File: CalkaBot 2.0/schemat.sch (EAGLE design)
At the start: 57 parts, among them IC1 TB6612FNG, IC2 LM339D, IC3 7806DT, Q1 16MHz, X1 MINI-USB_4P-85-32004-40X

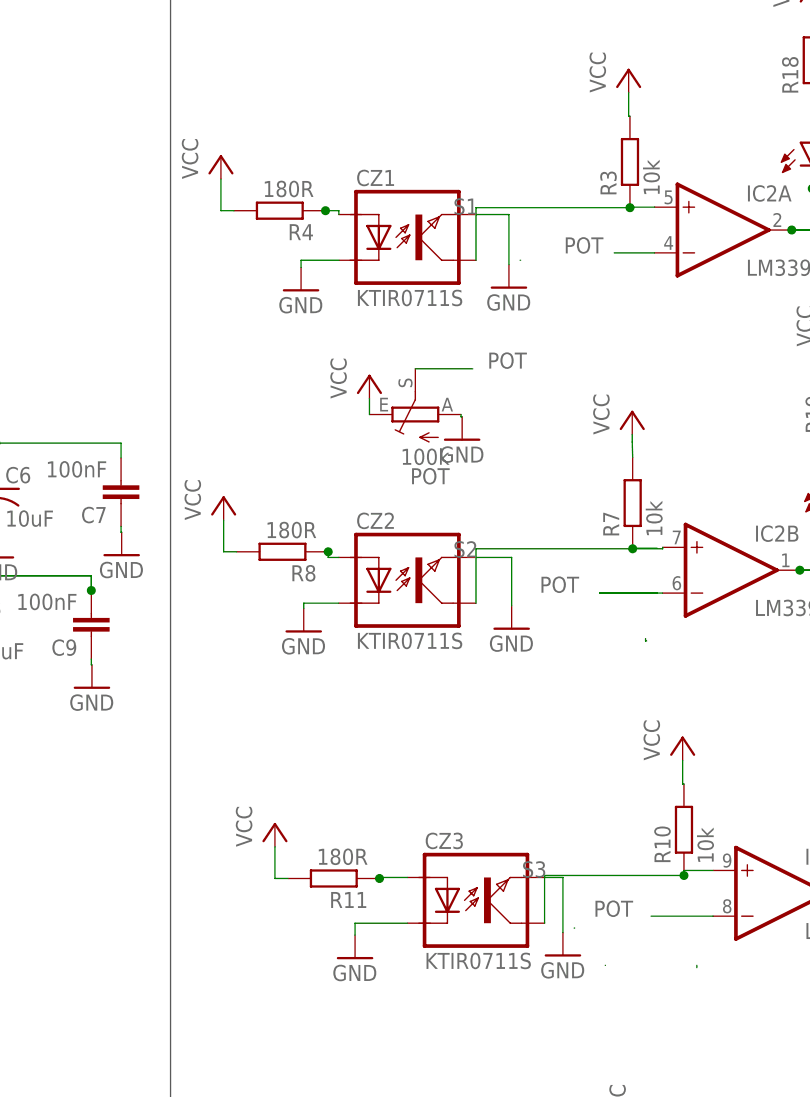
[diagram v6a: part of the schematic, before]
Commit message: Podłączone transoptory, trzeba rozkminić jak podłączyć gniazda
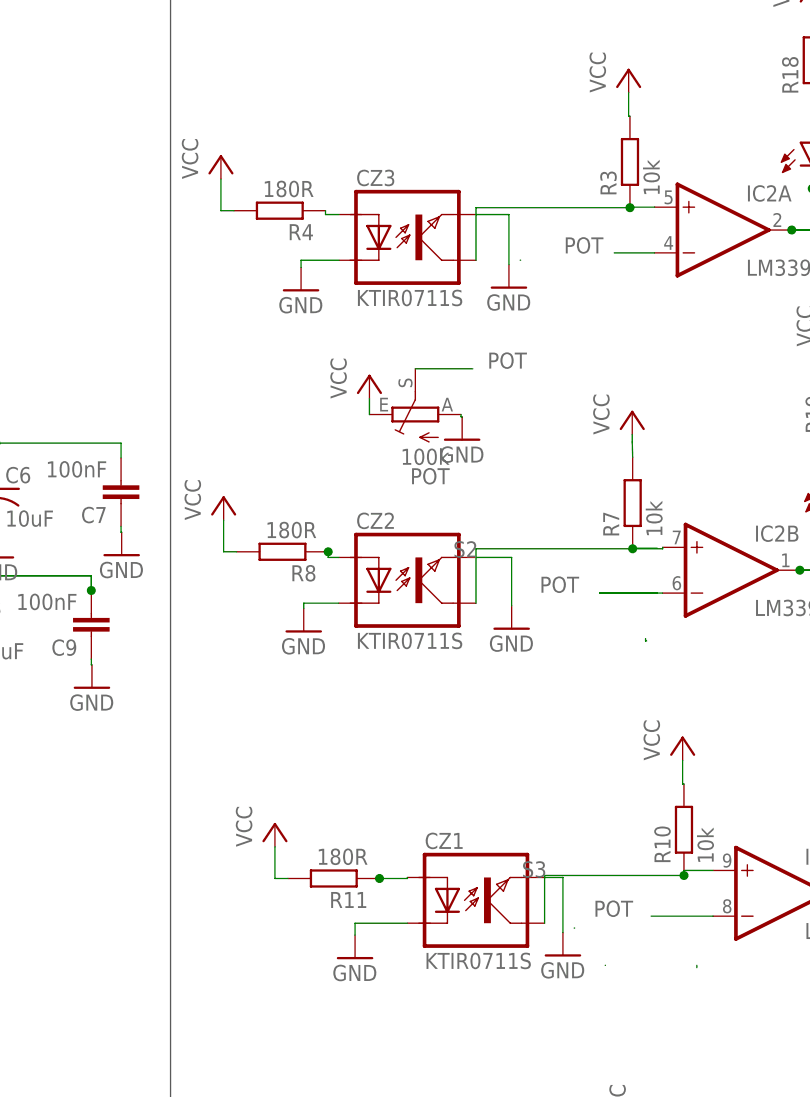
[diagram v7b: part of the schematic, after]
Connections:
- removed net S1: CZ1.KOLEKTOR, IC2A.+IN, R3.1
- new net N$14: CZ3.ANODA, R4.1
- net N$1: now also CZ3.KOLEKTOR, IC2A.+IN, R3.1; no longer CZ1.ANODA, R4.1
- net N$23: now also CZ1.ANODA; no longer CZ3.ANODA
- net S3: now also CZ1.KOLEKTOR; no longer CZ3.KOLEKTOR
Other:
- moved on the sheet: CZ1, CZ3
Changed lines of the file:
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@@
 <attribute name="VALUE" x="-127" y="20.32" size="1.778" layer="96"/>
 </instance>
-<instance part="CZ1" gate="G$1" x="185.42" y="106.68" smashed="yes">
-<attribute name="NAME" x="179.705" y="112.395" size="1.778" layer="95"/>
-<attribute name="VALUE" x="179.705" y="99.06" size="1.778" layer="96"/>
+<instance part="CZ1" gate="G$1" x="193.04" y="33.02" smashed="yes">
+<attribute name="NAME" x="187.325" y="38.735" size="1.778" layer="95"/>
+<attribute name="VALUE" x="187.325" y="25.4" size="1.778" layer="96"/>
 </instance>
 <instance part="CZ2" gate="G$1" x="185.42" y="68.58" smashed="yes">
@@
 <attribute name="VALUE" x="179.705" y="60.96" size="1.778" layer="96"/>
 </instance>
-<instance part="CZ3" gate="G$1" x="193.04" y="33.02" smashed="yes">
-<attribute name="NAME" x="187.325" y="38.735" size="1.778" layer="95"/>
-<attribute name="VALUE" x="187.325" y="25.4" size="1.778" layer="96"/>
+<instance part="CZ3" gate="G$1" x="185.42" y="106.68" smashed="yes">
+<attribute name="NAME" x="179.705" y="112.395" size="1.778" layer="95"/>
+<attribute name="VALUE" x="179.705" y="99.06" size="1.778" layer="96"/>
 </instance>
 <instance part="CZ4" gate="G$1" x="187.96" y="-7.62" smashed="yes">
@@
 </segment>
 <segment>
-<pinref part="CZ1" gate="G$1" pin="EMITER"/>
 <pinref part="GND3" gate="1" pin="GND"/>
-<wire x1="193.04" y1="109.22" x2="196.7" y2="109.22" width="0.1524" layer="91"/>
-<wire x1="196.7" y1="109.22" x2="196.7" y2="103.64" width="0.1524" layer="91"/>
+<pinref part="CZ3" gate="G$1" pin="EMITER"/>
+<wire x1="196.7" y1="103.64" x2="196.7" y2="109.22" width="0.1524" layer="91"/>
+<wire x1="196.7" y1="109.22" x2="193.04" y2="109.22" width="0.1524" layer="91"/>
 </segment>
 <segment>
 <pinref part="GND2" gate="1" pin="GND"/>
-<pinref part="CZ1" gate="G$1" pin="KATODA"/>
-<wire x1="173.6" y1="103.34" x2="173.6" y2="104.14" width="0.1524" layer="91"/>
-<wire x1="173.6" y1="104.14" x2="177.8" y2="104.14" width="0.1524" layer="91"/>
+<pinref part="CZ3" gate="G$1" pin="KATODA"/>
+<wire x1="177.8" y1="104.14" x2="173.6" y2="104.14" width="0.1524" layer="91"/>
+<wire x1="173.6" y1="104.14" x2="173.6" y2="103.34" width="0.1524" layer="91"/>
 </segment>
 <segment>
@@
 <segment>
 <pinref part="GND8" gate="1" pin="GND"/>
-<pinref part="CZ3" gate="G$1" pin="KATODA"/>
-<wire x1="179.6" y1="29.14" x2="179.6" y2="30.48" width="0.1524" layer="91"/>
-<wire x1="179.6" y1="30.48" x2="185.42" y2="30.48" width="0.1524" layer="91"/>
-</segment>
-<segment>
-<pinref part="CZ3" gate="G$1" pin="EMITER"/>
+<pinref part="CZ1" gate="G$1" pin="KATODA"/>
+<wire x1="185.42" y1="30.48" x2="179.6" y2="30.48" width="0.1524" layer="91"/>
+<wire x1="179.6" y1="30.48" x2="179.6" y2="29.14" width="0.1524" layer="91"/>
+</segment>
+<segment>
 <pinref part="GND9" gate="1" pin="GND"/>
+<pinref part="CZ1" gate="G$1" pin="EMITER"/>
 <wire x1="200.66" y1="35.56" x2="202.7" y2="35.56" width="0.1524" layer="91"/>
 <wire x1="202.7" y1="35.56" x2="202.7" y2="29.44" width="0.1524" layer="91"/>
@@
 </segment>
 </net>
-<net name="N$1" class="0">
-<segment>
-<pinref part="R4" gate="G$1" pin="1"/>
-<wire x1="176.318" y1="109.648" x2="176.318" y2="109.64" width="0.1524" layer="91"/>
-<pinref part="CZ1" gate="G$1" pin="ANODA"/>
-<wire x1="177.8" y1="109.22" x2="177.8" y2="109.648" width="0.1524" layer="91"/>
-<wire x1="177.8" y1="109.648" x2="176.318" y2="109.648" width="0.1524" layer="91"/>
-<junction x="176.318" y="109.648"/>
-</segment>
-</net>
-<net name="S1" class="0">
-<segment>
-<pinref part="IC2" gate="A" pin="+IN"/>
-<pinref part="R3" gate="G$1" pin="1"/>
-<wire x1="212.88" y1="110.04" x2="210.148" y2="110.04" width="0.1524" layer="91"/>
-<wire x1="210.148" y1="110.04" x2="210.148" y2="109.982" width="0.1524" layer="91"/>
-<wire x1="210.148" y1="109.64" x2="210.148" y2="109.982" width="0.1524" layer="91"/>
-<junction x="210.148" y="109.982"/>
-<label x="190.5" y="109.22" size="1.778" layer="95"/>
-<pinref part="CZ1" gate="G$1" pin="KOLEKTOR"/>
-<wire x1="193.04" y1="104.14" x2="193.04" y2="109.982" width="0.1524" layer="91"/>
-<wire x1="193.04" y1="109.982" x2="210.148" y2="109.982" width="0.1524" layer="91"/>
-</segment>
-</net>
 <net name="FL1" class="0">
 <segment>
@@
 <pinref part="R11" gate="G$1" pin="1"/>
 <wire x1="182.318" y1="35.448" x2="182.318" y2="35.44" width="0.1524" layer="91"/>
-<pinref part="CZ3" gate="G$1" pin="ANODA"/>
 <wire x1="182.318" y1="35.448" x2="182.318" y2="35.56" width="0.1524" layer="91"/>
-<wire x1="182.318" y1="35.56" x2="185.42" y2="35.56" width="0.1524" layer="91"/>
 <junction x="182.318" y="35.448"/>
+<pinref part="CZ1" gate="G$1" pin="ANODA"/>
+<wire x1="182.318" y1="35.448" x2="185.42" y2="35.448" width="0.1524" layer="91"/>
+<wire x1="185.42" y1="35.448" x2="185.42" y2="35.56" width="0.1524" layer="91"/>
 </segment>
 </net>
@@
 <wire x1="216.148" y1="36.34" x2="219.38" y2="36.34" width="0.1524" layer="91"/>
 <label x="198.12" y="35.56" size="1.778" layer="95"/>
-<pinref part="CZ3" gate="G$1" pin="KOLEKTOR"/>
+<pinref part="CZ1" gate="G$1" pin="KOLEKTOR"/>
 <wire x1="200.66" y1="30.48" x2="200.66" y2="35.782" width="0.1524" layer="91"/>
 <wire x1="200.66" y1="35.782" x2="216.148" y2="35.782" width="0.1524" layer="91"/>
@@
 </segment>
 </net>
+<net name="N$1" class="0">
+<segment>
+<pinref part="R3" gate="G$1" pin="1"/>
+<pinref part="IC2" gate="A" pin="+IN"/>
+<wire x1="212.88" y1="110.04" x2="210.148" y2="110.04" width="0.1524" layer="91"/>
+<wire x1="210.148" y1="110.04" x2="210.148" y2="109.982" width="0.1524" layer="91"/>
+<wire x1="210.148" y1="109.64" x2="210.148" y2="109.982" width="0.1524" layer="91"/>
+<junction x="210.148" y="109.982"/>
+<pinref part="CZ3" gate="G$1" pin="KOLEKTOR"/>
+<wire x1="193.04" y1="104.14" x2="193.04" y2="109.982" width="0.1524" layer="91"/>
+<wire x1="193.04" y1="109.982" x2="210.148" y2="109.982" width="0.1524" layer="91"/>
+</segment>
+</net>
+<net name="N$14" class="0">
+<segment>
+<pinref part="R4" gate="G$1" pin="1"/>
+<pinref part="CZ3" gate="G$1" pin="ANODA"/>
+<wire x1="176.318" y1="109.648" x2="176.318" y2="109.22" width="0.1524" layer="91"/>
+<wire x1="176.318" y1="109.22" x2="177.8" y2="109.22" width="0.1524" layer="91"/>
+</segment>
+</net>

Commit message: Ładnie opisane od góry
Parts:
- added L7: (no value), led:LEDCHIP-LED0805
- added M1A, M1B, M2A, M2B: (no value), pinhead:PINHD-1X1
- added R24: 220R, rcl:R-EU_R0805
- renumbered JP1 to VCC, JP3 to ICSP, LED5 to 5V, LED6 to ON, LED7 to K, RESETBUTTON to RESET, SW2 to DRIVE, X1 to USB
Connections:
- new net N$18: L7.A, R24.1
- net AO1: now also M1A.1
- net AO2: now also M2B.1
- net BO1: now also M1B.1
- net BO2: now also M2A.1
- net GND: now also L7.C
- net I/O11: now also R24.2
